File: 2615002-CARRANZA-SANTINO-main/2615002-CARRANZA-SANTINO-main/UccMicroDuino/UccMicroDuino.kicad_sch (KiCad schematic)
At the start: 14 parts, among them J1 USB_A, J2 Header, U1 ATtiny85-20SU

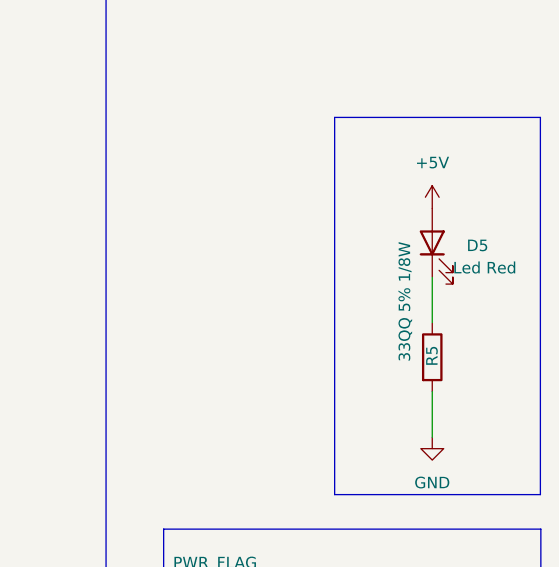
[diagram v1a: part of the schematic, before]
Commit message: 2615002-mi primer versionado de gitbash (correccion placa)
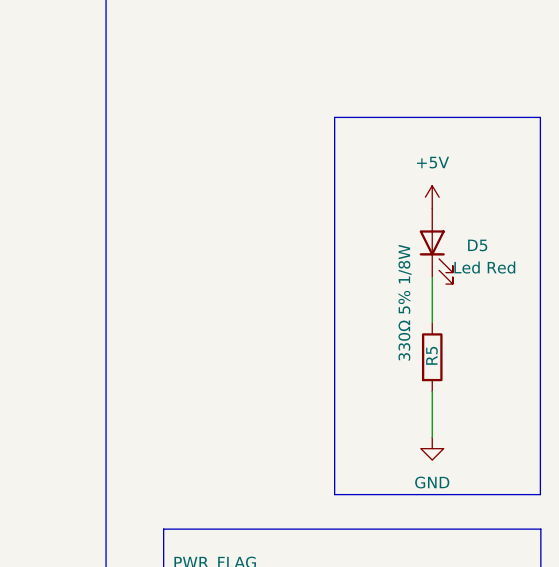
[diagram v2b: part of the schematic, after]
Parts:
- D1: footprint Diode_SMD:D_MELF_Handsoldering -> Diode_SMD:D_SOD-123
- D3: footprint Diode_SMD:D_SOD-123 -> Diode_SMD:D_MiniMELF
- R5: value 33QQ 5% 1/8W -> 330Ω 5% 1/8W
- U1: footprint Package_SO:SOIC-8W_5.3x5.3mm_P1.27mm -> Package_SO:SOIC-8_5.3x5.3mm_P1.27mm
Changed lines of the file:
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@@
 			)
 		)
-		(property "Footprint" "Diode_SMD:D_MELF_Handsoldering"
+		(property "Footprint" "Diode_SMD:D_SOD-123"
 			(at 86.36 109.22 0)
 			(hide yes)
@@
 			)
 		)
-		(property "Footprint" "Package_SO:SOIC-8W_5.3x5.3mm_P1.27mm"
+		(property "Footprint" "Package_SO:SOIC-8_5.3x5.3mm_P1.27mm"
 			(at 173.99 120.65 0)
 			(hide yes)
@@
 			)
 		)
-		(property "Footprint" "Diode_SMD:D_SOD-123"
+		(property "Footprint" "Diode_SMD:D_MiniMELF"
 			(at 76.2 78.74 0)
 			(hide yes)
@@
 			)
 		)
-		(property "Value" "33QQ 5% 1/8W"
+		(property "Value" "330Ω 5% 1/8W"
 			(at 254.762 89.408 90)
 			(show_name no)
